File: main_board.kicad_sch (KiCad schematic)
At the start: 100 parts, among them CN10 DF40C-40DP-0.4V, CN11 DF40C-30DP-0.4V, CN19 DF40C-24DP-0.4V, CN2 DF40C-50DP-0.4V, CN8 DF40C-40DP-0.4V, J4 DF40C-100DP-0.4V51*2, Q4 MMBT3904-C20526, SW1 SW_Push, SW2 SW_Push, U11 SiP32508DT, U47 ES8388, U48 TS5A23157DGSR, U49 TS5A23157DGSR, U50 PAM8302AASCR, U51 PAM8302AASCR, U52 TPS7A0233PDBVR, U62 PCA9306DCUR, U63 AP2120N-2.8TRG1, U65 MSM381ADB001, U66 DF40B-10DS-0.4V, U67 SIP32508DT-T1-GE3, U68 SN74AHCT125PWR, U69 TCA9535PWR, U8 ESD7104MUTAG_C2987068

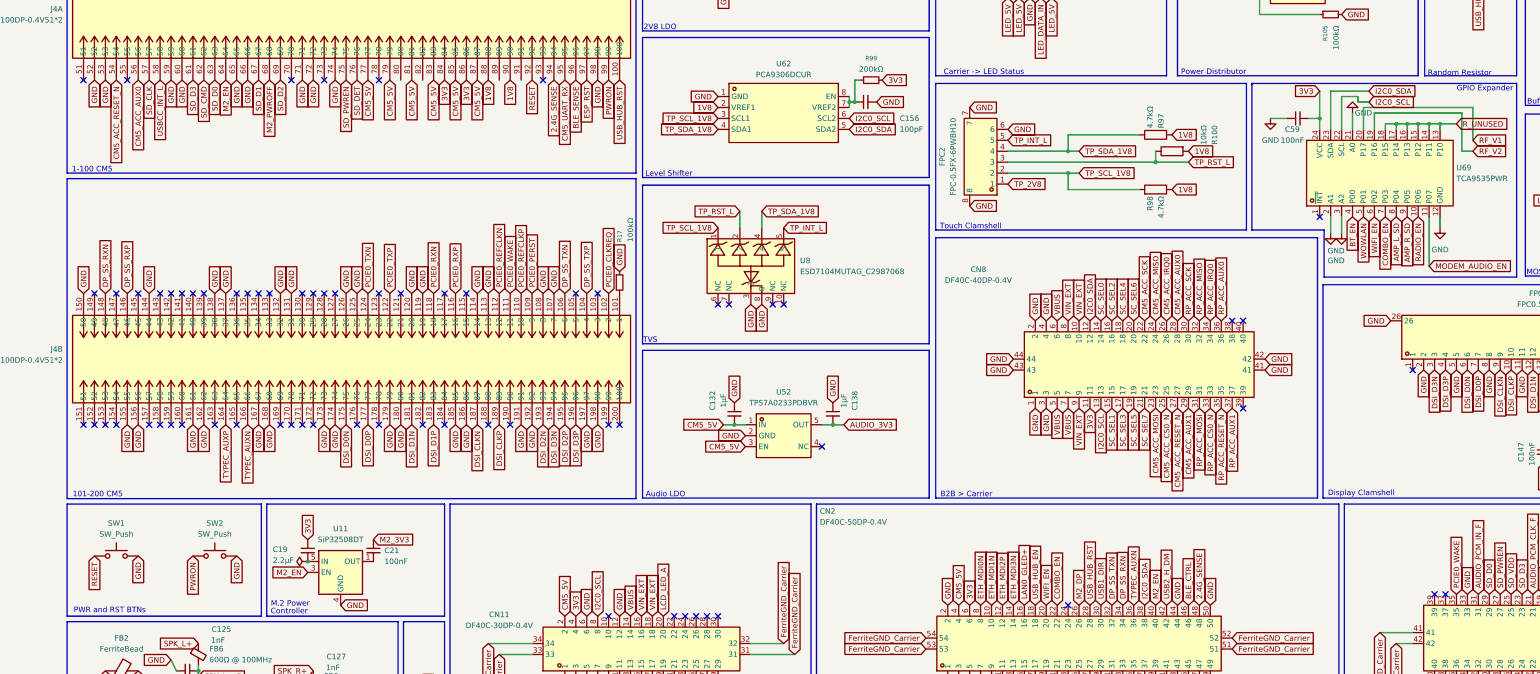
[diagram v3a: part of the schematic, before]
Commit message: continued work on carrier board, started work on m.2 board
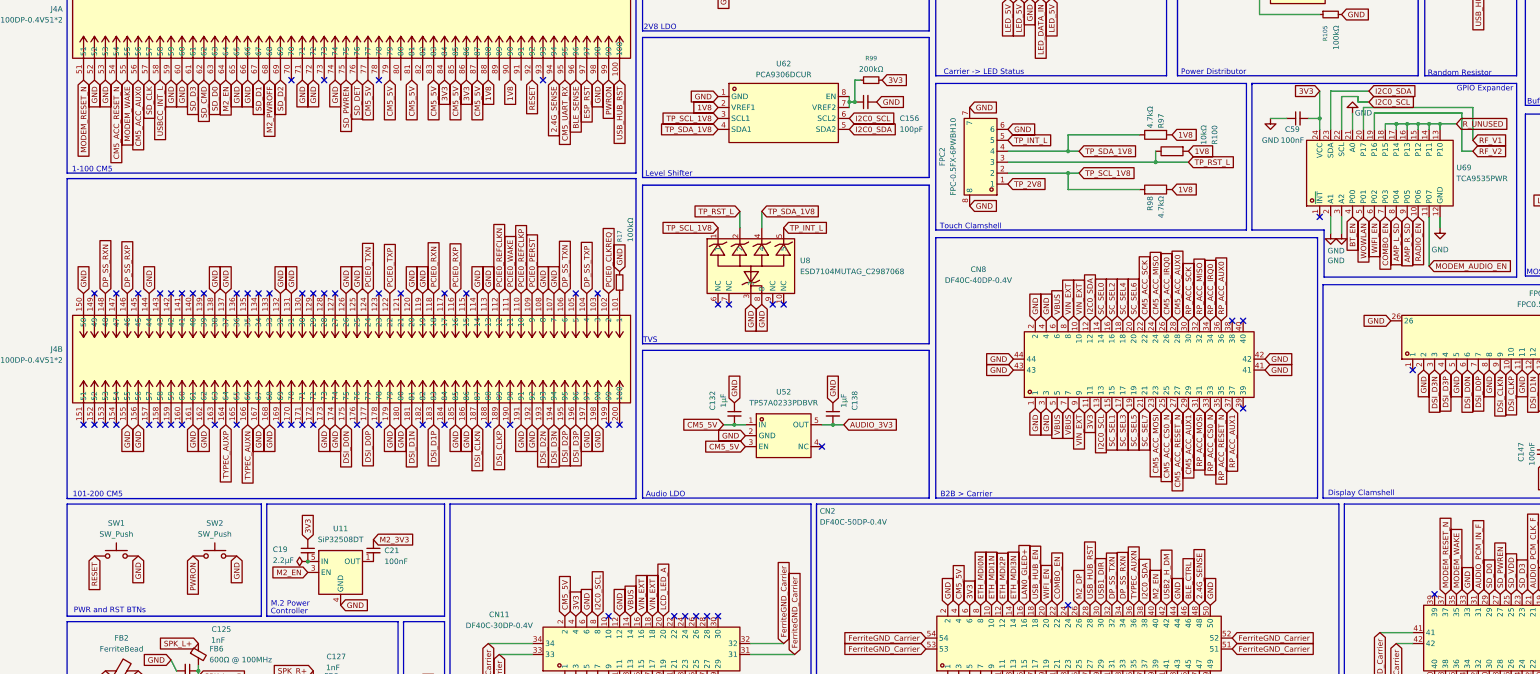
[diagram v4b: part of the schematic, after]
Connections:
- net PCIE0_WAKE: no longer CN10.35
- net MODEM_RESET_N: now reaches J4.51
- net MODEM_RESET_N: now also CN10.37
- net MODEM_WAKE: now reaches J4.55
- net MODEM_WAKE: now also CN10.35
- no-connect marks 90 -> 87
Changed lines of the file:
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@@
 	)
 	(no_connect
-		(at 398.78 247.65)
-	)
-	(no_connect
 		(at 130.81 128.27)
 	)
@@
 	)
 	(no_connect
-		(at 92.71 128.27)
-	)
-	(no_connect
 		(at 151.13 177.8)
 	)
@@
 	)
 	(no_connect
-		(at 82.55 128.27)
-	)
-	(no_connect
 		(at 254 213.36)
 	)
@@
 		)
 	)
+	(global_label "MODEM_WAKE"
+		(shape input)
+		(at 401.32 247.65 90)
+		(fields_autoplaced yes)
+		(effects
+			(font
+				(size 1.27 1.27)
+			)
+			(justify left)
+		)
+		(property "Intersheetrefs" "${INTERSHEET_REFS}"
+			(at 401.32 232.0859 90)
+			(hide yes)
+			(show_name no)
+			(do_not_autoplace no)
+			(effects
+				(font
+					(size 1.27 1.27)
+				)
+				(justify left)
+			)
+		)
+	)
 	(global_label "GND"
 		(shape input)
@@
 		)
 	)
-	(global_label "PCIE0_WAKE"
-		(shape input)
-		(at 401.32 247.65 90)
-		(fields_autoplaced yes)
-		(effects
-			(font
-				(size 1.27 1.27)
-			)
-			(justify left)
-		)
-		(property "Intersheetrefs" "${INTERSHEET_REFS}"
-			(at 401.32 233.2349 90)
-			(hide yes)
-			(show_name no)
-			(do_not_autoplace no)
-			(effects
-				(font
-					(size 1.27 1.27)
-				)
-				(justify left)
-			)
-		)
-	)
 	(global_label "GND"
 		(shape input)
@@
 		)
 	)
+	(global_label "MODEM_RESET_N"
+		(shape input)
+		(at 82.55 128.27 270)
+		(fields_autoplaced yes)
+		(effects
+			(font
+				(size 1.27 1.27)
+			)
+			(justify right)
+		)
+		(property "Intersheetrefs" "${INTERSHEET_REFS}"
+			(at 82.55 146.9183 90)
+			(hide yes)
+			(show_name no)
+			(do_not_autoplace no)
+			(effects
+				(font
+					(size 1.27 1.27)
+				)
+				(justify right)
+			)
+		)
+	)
 	(global_label "GND"
 		(shape input)
@@
 		)
 	)
+	(global_label "MODEM_WAKE"
+		(shape input)
+		(at 92.71 128.27 270)
+		(fields_autoplaced yes)
+		(effects
+			(font
+				(size 1.27 1.27)
+			)
+			(justify right)
+		)
+		(property "Intersheetrefs" "${INTERSHEET_REFS}"
+			(at 92.71 143.8341 90)
+			(hide yes)
+			(show_name no)
+			(do_not_autoplace no)
+			(effects
+				(font
+					(size 1.27 1.27)
+				)
+				(justify right)
+			)
+		)
+	)
 	(global_label "FerriteGND_Carrier"
 		(shape input)
@@
 			)
 		)
+	)
+	(global_label "MODEM_RESET_N"
+		(shape input)
+		(at 398.78 247.65 90)
+		(fields_autoplaced yes)
+		(effects
+			(font
+				(size 1.27 1.27)
+			)
+			(justify left)
+		)
+		(property "Intersheetrefs" "${INTERSHEET_REFS}"
+			(at 398.78 229.0017 90)
+			(hide yes)
+			(show_name no)
+			(do_not_autoplace no)
+			(effects
+				(font
+					(size 1.27 1.27)
+				)
+				(justify left)
+			)
+		)

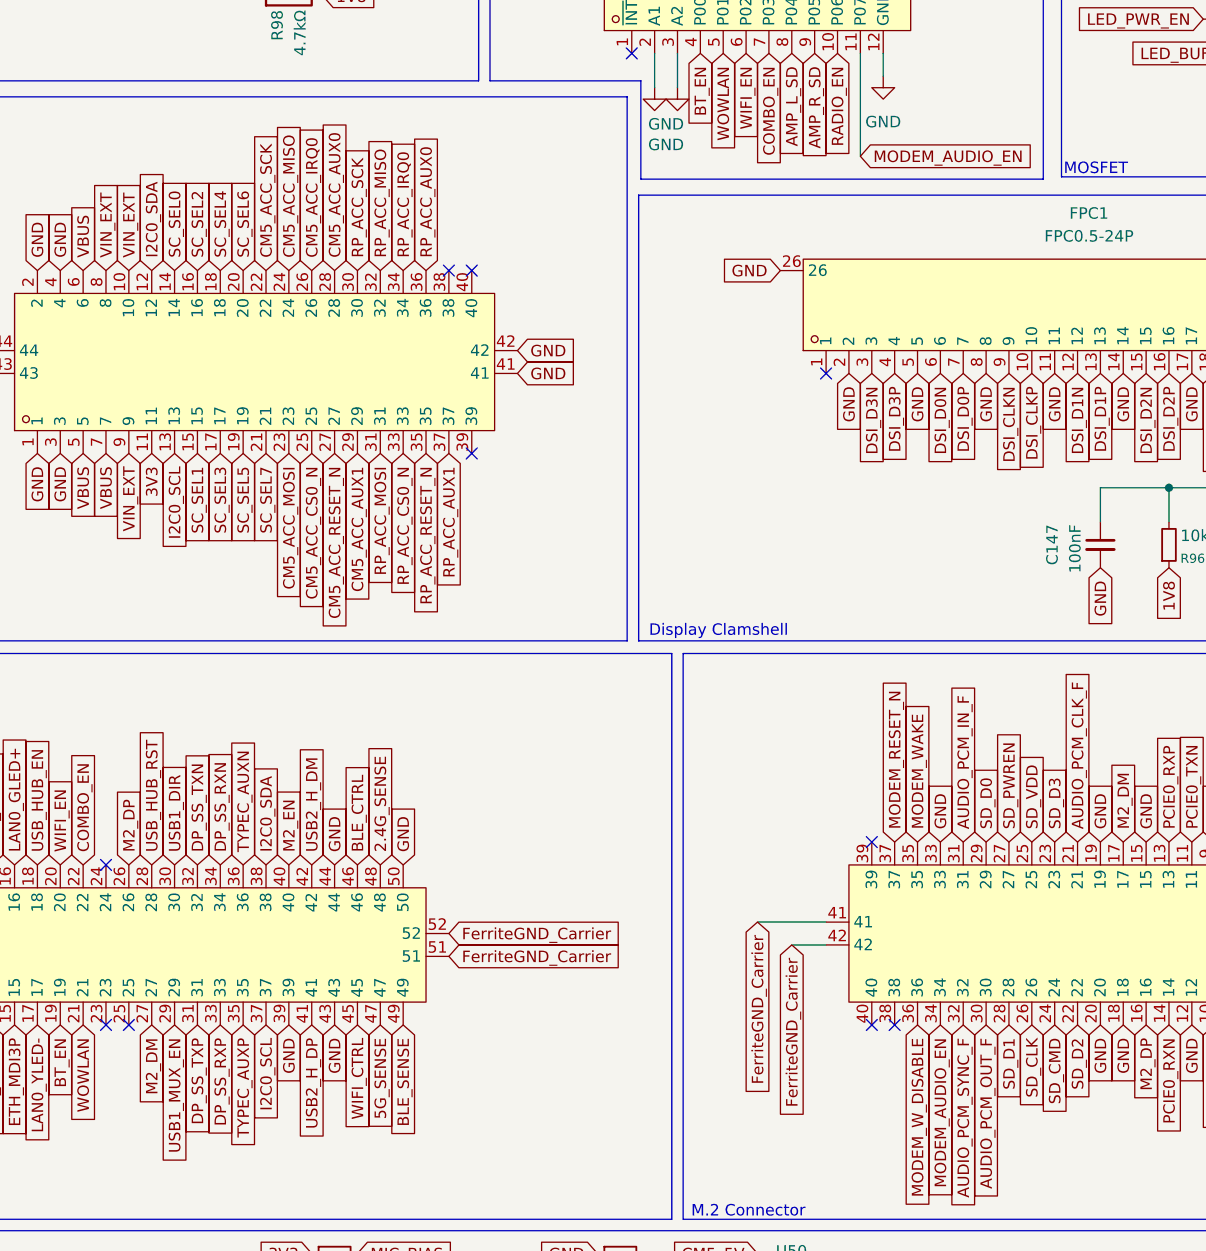
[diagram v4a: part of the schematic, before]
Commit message: finished m.2 board and copper pours, completed antenna bracket and power board, finished slateconnect board, reorganized libraries
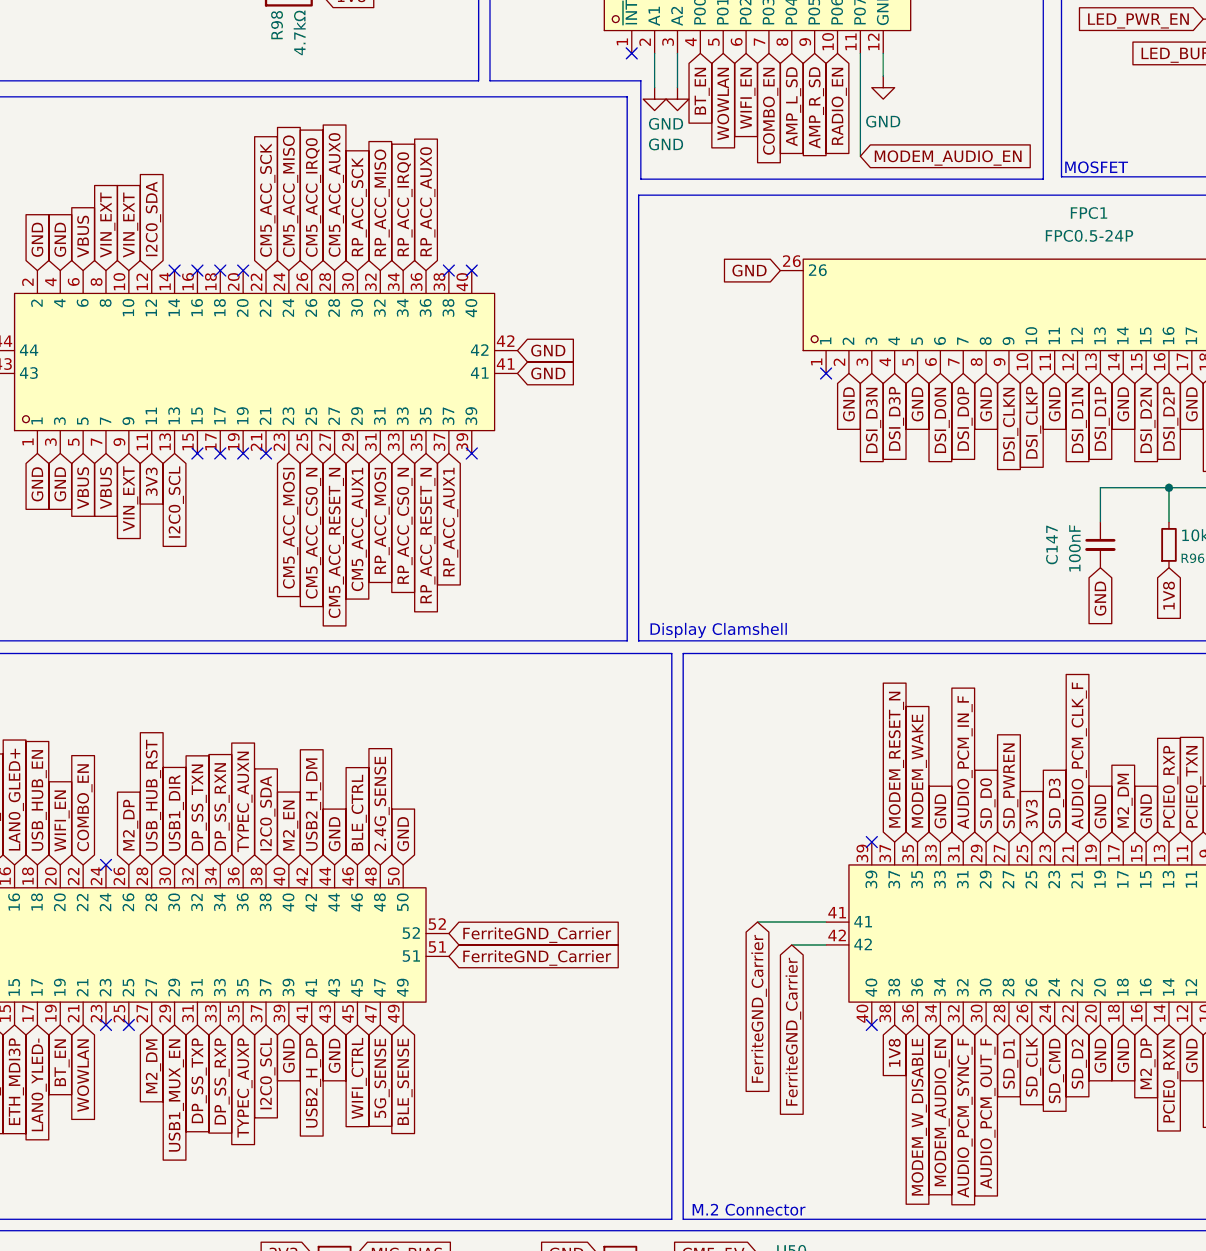
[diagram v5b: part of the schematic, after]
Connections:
- net SD_VDD is gone; now on net 3V3: CN10.25
- net 1V8: now also CN10.38
- net SC_SEL0: no longer names the net of CN8.14
- net SC_SEL1: no longer names the net of CN8.15
- net SC_SEL2: no longer names the net of CN8.16
- net SC_SEL3: no longer names the net of CN8.17
- net SC_SEL4: no longer names the net of CN8.18
- net SC_SEL5: no longer names the net of CN8.19
- net SC_SEL6: no longer names the net of CN8.20
- net SC_SEL7: no longer names the net of CN8.21
- no-connect marks 87 -> 94
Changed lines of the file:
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@@
 	)
 	(no_connect
+		(at 321.31 184.15)
+	)
+	(no_connect
+		(at 204.47 252.73)
+	)
+	(no_connect
 		(at 130.81 128.27)
 	)
@@
 	)
 	(no_connect
+		(at 326.39 204.47)
+	)
+	(no_connect
 		(at 176.53 208.28)
 	)
@@
 	)
 	(no_connect
-		(at 398.78 267.97)
-	)
-	(no_connect
 		(at 219.71 252.73)
 	)
 	(no_connect
-		(at 396.24 267.97)
-	)
-	(no_connect
 		(at 227.33 252.73)
 	)
@@
 	)
 	(no_connect
+		(at 323.85 204.47)
+	)
+	(no_connect
 		(at 351.79 204.47)
 	)
@@
 	)
 	(no_connect
+		(at 326.39 184.15)
+	)
+	(no_connect
 		(at 417.83 312.42)
 	)
@@
 	)
 	(no_connect
+		(at 323.85 184.15)
+	)
+	(no_connect
 		(at 128.27 208.28)
 	)
@@
 	)
 	(no_connect
+		(at 321.31 204.47)
+	)
+	(no_connect
 		(at 223.52 313.69)
 	)
@@
 	)
 	(no_connect
-		(at 204.47 252.73)
-	)
-	(no_connect
 		(at 457.2 107.95)
 	)
@@
 	)
 	(no_connect
-		(at 396.24 247.65)
-	)
-	(no_connect
 		(at 90.17 208.28)
 	)
@@
 	)
 	(no_connect
+		(at 396.24 267.97)
+	)
+	(no_connect
 		(at 349.25 184.15)
 	)
@@
 	)
 	(no_connect
+		(at 396.24 247.65)
+	)
+	(no_connect
 		(at 222.25 267.97)
 	)
@@
 	)
 	(no_connect
+		(at 328.93 204.47)
+	)
+	(no_connect
 		(at 391.16 195.58)
 	)
 	(no_connect
+		(at 318.77 184.15)
+	)
+	(no_connect
 		(at 369.57 160.02)
 	)
@@
 		)
 	)
-	(global_label "SD_VDD"
+	(global_label "3V3"
 		(shape input)
 		(at 414.02 247.65 90)
@@
 		)
 		(property "Intersheetrefs" "${INTERSHEET_REFS}"
-			(at 414.02 237.5891 90)
+			(at 414.02 241.1572 90)
 			(hide yes)
 			(show_name no)
@@
 		)
 	)
-	(global_label "SC_SEL7"
-		(shape input)
-		(at 328.93 204.47 270)
-		(fields_autoplaced yes)
-		(effects
-			(font
-				(size 1.27 1.27)
-			)
-			(justify right)
-		)
-		(property "Intersheetrefs" "${INTERSHEET_REFS}"
-			(at 328.93 215.4984 90)
-			(hide yes)
-			(show_name no)
-			(do_not_autoplace no)
-			(effects
-				(font
-					(size 1.27 1.27)
-				)
-				(justify right)
-			)
-		)
-	)
 	(global_label "GND"
 		(shape input)
@@
 		)
 	)
-	(global_label "SC_SEL0"
+	(global_label "GND"
 		(shape input)
-		(at 318.77 184.15 90)
+		(at 191.77 177.8 90)
 		(fields_autoplaced yes)
 		(effects
@@
 		)
 		(property "Intersheetrefs" "${INTERSHEET_REFS}"
-			(at 318.77 173.1216 90)
+			(at 191.77 170.9443 90)
 			(hide yes)
 			(show_name no)
@@
 		)
 	)
-	(global_label "GND"
+	(global_label "3V3"
 		(shape input)
-		(at 191.77 177.8 90)
+		(at 134.62 234.95 90)
 		(fields_autoplaced yes)
 		(effects
@@
 		)
 		(property "Intersheetrefs" "${INTERSHEET_REFS}"
-			(at 191.77 170.9443 90)
+			(at 134.62 228.4572 90)
 			(hide yes)
 			(show_name no)
@@
 		)
 	)
-	(global_label "3V3"
+	(global_label "LED_PWR_EN"
 		(shape input)
-		(at 134.62 234.95 90)
+		(at 355.6 107.95 180)
 		(fields_autoplaced yes)
 		(effects
@@
 				(size 1.27 1.27)
 			)
-			(justify left)
+			(justify right)
 		)
 		(property "Intersheetrefs" "${INTERSHEET_REFS}"
-			(at 134.62 228.4572 90)
+			(at 340.7616 107.95 0)
 			(hide yes)
 			(show_name no)
@@
 					(size 1.27 1.27)
 				)
-				(justify left)
+				(justify right)
 			)
 		)
 	)
-	(global_label "LED_PWR_EN"
+	(global_label "MODEM_AUDIO_EN"
 		(shape input)
-		(at 355.6 107.95 180)
+		(at 280.67 300.99 180)
 		(fields_autoplaced yes)
 		(effects
@@
 		)
 		(property "Intersheetrefs" "${INTERSHEET_REFS}"
-			(at 340.7616 107.95 0)
+			(at 260.9934 300.99 0)
 			(hide yes)
 			(show_name no)
@@
 		)
 	)
-	(global_label "MODEM_AUDIO_EN"
+	(global_label "1V8"
 		(shape input)
-		(at 280.67 300.99 180)
+		(at 398.78 267.97 270)
 		(fields_autoplaced yes)
 		(effects
@@
 		)
 		(property "Intersheetrefs" "${INTERSHEET_REFS}"
-			(at 260.9934 300.99 0)
+			(at 398.78 274.4628 90)
 			(hide yes)
 			(show_name no)
@@
 		)
 	)
-	(global_label "SC_SEL2"
-		(shape input)
-		(at 321.31 184.15 90)
-		(fields_autoplaced yes)
-		(effects
-			(font
-				(size 1.27 1.27)
-			)
-			(justify left)
-		)
-		(property "Intersheetrefs" "${INTERSHEET_REFS}"
-			(at 321.31 173.1216 90)
-			(hide yes)
-			(show_name no)
-			(do_not_autoplace no)
-			(effects
-				(font
-					(size 1.27 1.27)
-				)
-				(justify left)
-			)
-		)
-	)
 	(global_label "GND"
 		(shape input)
@@
 		)
 	)
-	(global_label "SC_SEL4"
-		(shape input)
-		(at 323.85 184.15 90)
-		(fields_autoplaced yes)
-		(effects
-			(font
-				(size 1.27 1.27)
-			)
-			(justify left)
-		)
-		(property "Intersheetrefs" "${INTERSHEET_REFS}"
-			(at 323.85 173.1216 90)
-			(hide yes)
-			(show_name no)
-			(do_not_autoplace no)
-			(effects
-				(font
-					(size 1.27 1.27)
-				)
-				(justify left)
-			)
-		)
-	)
 	(global_label "LED_PWR_EN"
 		(shape input)
@@
 		)
 	)
-	(global_label "SC_SEL3"
-		(shape input)
-		(at 323.85 204.47 270)
-		(fields_autoplaced yes)
-		(effects
-			(font
-				(size 1.27 1.27)
-			)
-			(justify right)
-		)
-		(property "Intersheetrefs" "${INTERSHEET_REFS}"
-			(at 323.85 215.4984 90)
-			(hide yes)
-			(show_name no)
-			(do_not_autoplace no)
-			(effects
-				(font
-					(size 1.27 1.27)
-				)
-				(justify right)
-			)
-		)
-	)
 	(global_label "GND"
 		(shape input)
@@
 		)
 	)
-	(global_label "SC_SEL1"
-		(shape input)
-		(at 321.31 204.47 270)
-		(fields_autoplaced yes)
-		(effects
-			(font
-				(size 1.27 1.27)
-			)
-			(justify right)
-		)
-		(property "Intersheetrefs" "${INTERSHEET_REFS}"
-			(at 321.31 215.4984 90)
-			(hide yes)
-			(show_name no)
-			(do_not_autoplace no)
-			(effects
-				(font
-					(size 1.27 1.27)
-				)
-				(justify right)
-			)
-		)
-	)
 	(global_label "DSI_CLKN"
 		(shape input)
@@
 		)
 	)
-	(global_label "SC_SEL6"
-		(shape input)
-		(at 326.39 184.15 90)
-		(fields_autoplaced yes)
-		(effects
-			(font
-				(size 1.27 1.27)
-			)
-			(justify left)
-		)
-		(property "Intersheetrefs" "${INTERSHEET_REFS}"
-			(at 326.39 173.1216 90)
-			(hide yes)
-			(show_name no)
-			(do_not_autoplace no)
-			(effects
-				(font
-					(size 1.27 1.27)
-				)
-				(justify left)
-			)
-		)
-	)
 	(global_label "GND"
 		(shape input)
@@
 			(hide yes)
 			(show_name no)
-			(do_not_autoplace no)
-			(effects
-				(font
-					(size 1.27 1.27)
-				)
-				(justify right)
-			)
-		)
-	)
-	(global_label "SC_SEL5"
-		(shape input)
-		(at 326.39 204.47 270)
-		(fields_autoplaced yes)
-		(effects
-			(font
-				(size 1.27 1.27)
-			)
-			(justify right)
-		)
-		(property "Intersheetrefs" "${INTERSHEET_REFS}"
-			(at 326.39 215.4984 90)
-			(hide yes)
-			(show_name no)
